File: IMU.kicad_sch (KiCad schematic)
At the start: 7 parts, among them U301 LIS3MDLTR, U302 LSM6DSOXTR

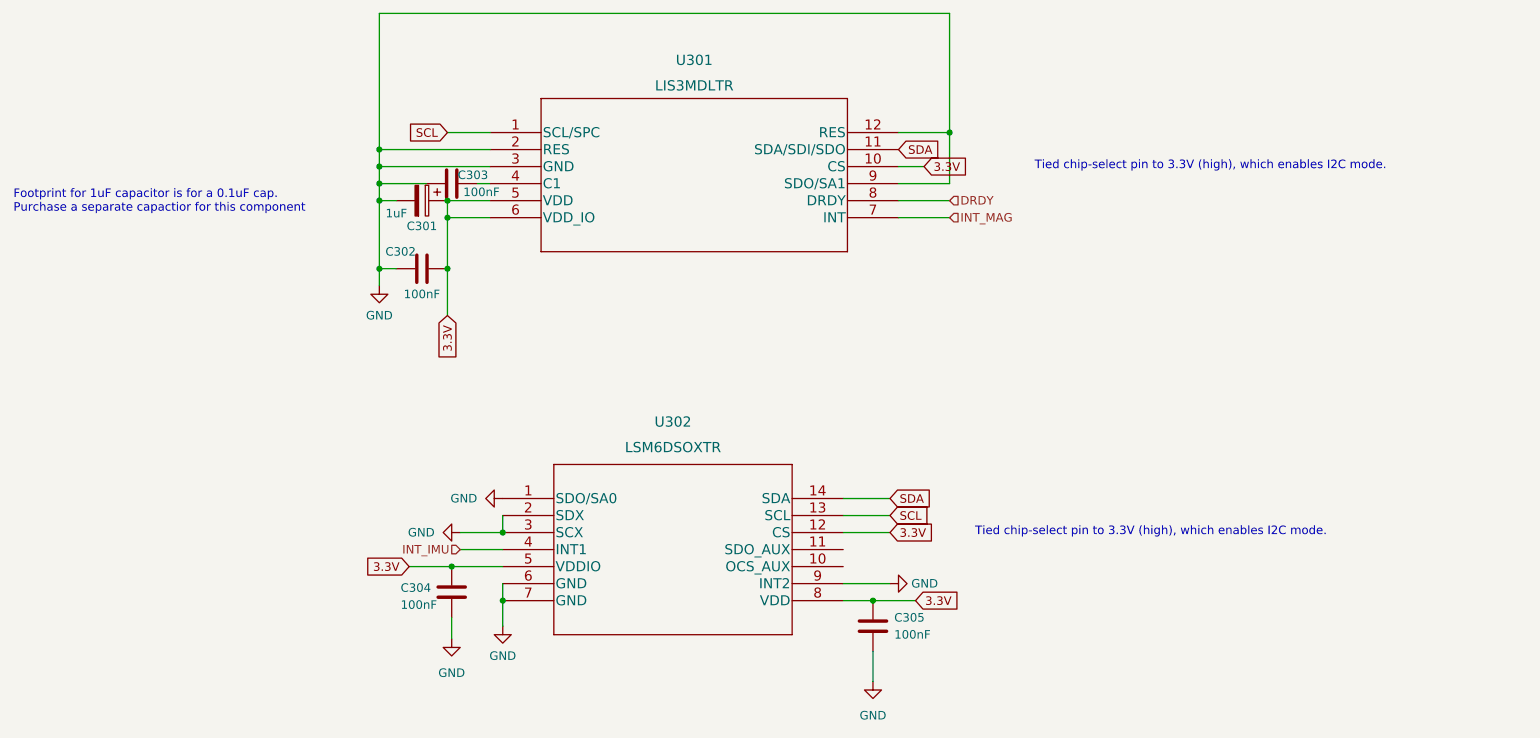
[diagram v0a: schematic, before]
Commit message: minor change to IMU schematic
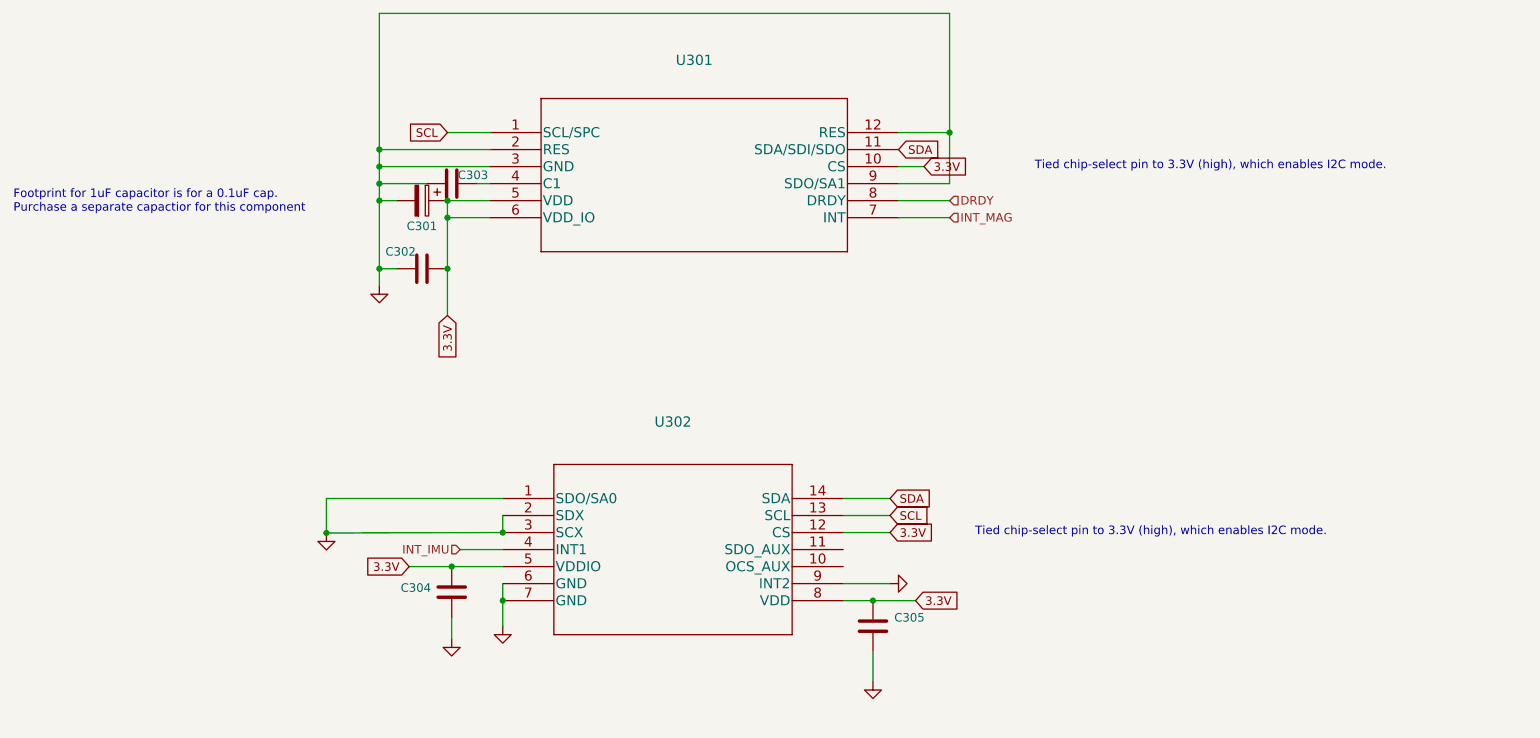
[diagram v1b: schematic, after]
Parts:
- C301: value 1uF -> (none); footprint 0.1uF P_Cap:UWP1H0R1MCL1GB -> (none)
- C302, C303, C304, C305: value 100nF -> (none); footprint Capacitor_SMD:C_0603_1608Metric_Pad1.08x0.95mm_HandSolder -> (none)
- U301: value LIS3MDLTR -> (none); footprint 3-axis magnetometer:LIS3MDLTR -> (none)
- U302: value LSM6DSOXTR -> (none); footprint 6-axis IMU:LSM6DSOXTR -> (none)
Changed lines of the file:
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@@
   (junction (at 105.41 137.795) (diameter 0) (color 0 0 0 0)
   )
+  (junction (at 79.0951 127.6916) (diameter 0) (color 0 0 0 0)
+  )
   (junction (at 105.41 127.635) (diameter 0) (color 0 0 0 0)
   )
@@
     (stroke (width 0) (type default) (color 0 0 0 0))
   )
+  (wire (pts (xy 105.41 122.555) (xy 79.0951 122.555))
+    (stroke (width 0) (type default) (color 0 0 0 0))
+  )
   (wire (pts (xy 156.21 135.255) (xy 163.195 135.255))
     (stroke (width 0) (type default) (color 0 0 0 0))
@@
     (stroke (width 0) (type default) (color 0 0 0 0))
   )
+  (wire (pts (xy 79.0951 122.555) (xy 79.0951 127.6916))
+    (stroke (width 0) (type default) (color 0 0 0 0))
+  )
   (wire (pts (xy 164.465 67.945) (xy 172.085 67.945))
     (stroke (width 0) (type default) (color 0 0 0 0))
@@
     (stroke (width 0) (type default) (color 0 0 0 0))
   )
-  (wire (pts (xy 99.06 127.635) (xy 105.41 127.635))
+  (wire (pts (xy 79.0951 127.6916) (xy 105.41 127.635))
     (stroke (width 0) (type default) (color 0 0 0 0))
   )
@@
     (in_bom yes) (on_board yes)
     (property "Reference" "C303" (id 0) (at 100.965 74.295 90))
-    (property "Value" "100nF" (id 1) (at 102.235 76.835 90))
-    (property "Footprint" "Capacitor_SMD:C_0603_1608Metric_Pad1.08x0.95mm_HandSolder" (id 2) (at 101.6 74.5998 0)
+    (property "Value" "" (id 1) (at 102.235 76.835 90))
+    (property "Footprint" "" (id 2) (at 101.6 74.5998 0)
       (effects (font (size 1.27 1.27)) hide)
     )
@@
       (effects (font (size 1.27 1.27)) (justify left))
     )
-    (property "Value" "100nF" (id 1) (at 163.83 142.8749 0)
+    (property "Value" "" (id 1) (at 163.83 142.8749 0)
       (effects (font (size 1.27 1.27)) (justify left))
     )
-    (property "Footprint" "Capacitor_SMD:C_0603_1608Metric_Pad1.08x0.95mm_HandSolder" (id 2) (at 161.6202 145.415 0)
+    (property "Footprint" "" (id 2) (at 161.6202 145.415 0)
       (effects (font (size 1.27 1.27)) hide)
     )
@@
     (pin "2")
   )
-  (symbol (lib_id "power:GND") (at 99.06 127.635 270) (unit 1)
-    (in_bom yes) (on_board yes) (fields_autoplaced)
-    (property "Reference" "#PWR0117" (id 0) (at 92.71 127.635 0)
-      (effects (font (size 1.27 1.27)) hide)
-    )
-    (property "Value" "GND" (id 1) (at 95.25 127.6349 90)
-      (effects (font (size 1.27 1.27)) (justify right))
-    )
-    (property "Footprint" "" (id 2) (at 99.06 127.635 0)
-      (effects (font (size 1.27 1.27)) hide)
-    )
-    (property "Datasheet" "" (id 3) (at 99.06 127.635 0)
-      (effects (font (size 1.27 1.27)) hide)
-    )
-    (pin "1")
-  )
-  (symbol (lib_id "power:GND") (at 105.41 122.555 270) (unit 1)
-    (in_bom yes) (on_board yes) (fields_autoplaced)
-    (property "Reference" "#PWR0122" (id 0) (at 99.06 122.555 0)
-      (effects (font (size 1.27 1.27)) hide)
-    )
-    (property "Value" "GND" (id 1) (at 101.6 122.5549 90)
-      (effects (font (size 1.27 1.27)) (justify right))
-    )
-    (property "Footprint" "" (id 2) (at 105.41 122.555 0)
-      (effects (font (size 1.27 1.27)) hide)
-    )
-    (property "Datasheet" "" (id 3) (at 105.41 122.555 0)
+  (symbol (lib_id "power:GND") (at 79.0951 127.6916 0) (unit 1)
+    (in_bom yes) (on_board yes) (fields_autoplaced)
+    (property "Reference" "#PWR0117" (id 0) (at 79.0951 134.0416 0)
+      (effects (font (size 1.27 1.27)) hide)
+    )
+    (property "Value" "" (id 1) (at 79.0951 132.2169 0))
+    (property "Footprint" "" (id 2) (at 79.0951 127.6916 0)
+      (effects (font (size 1.27 1.27)) hide)
+    )
+    (property "Datasheet" "" (id 3) (at 79.0951 127.6916 0)
       (effects (font (size 1.27 1.27)) hide)
     )
@@
       (effects (font (size 1.27 1.27)) hide)
     )
-    (property "Value" "GND" (id 1) (at 97.79 148.59 0))
+    (property "Value" "" (id 1) (at 97.79 148.59 0))
     (property "Footprint" "" (id 2) (at 97.79 143.51 0)
       (effects (font (size 1.27 1.27)) hide)
@@
       (effects (font (size 1.27 1.27)) (justify left))
     )
-    (property "Value" "100nF" (id 1) (at 90.17 138.43 0)
+    (property "Value" "" (id 1) (at 90.17 138.43 0)
       (effects (font (size 1.27 1.27)) (justify left))
     )
-    (property "Footprint" "Capacitor_SMD:C_0603_1608Metric_Pad1.08x0.95mm_HandSolder" (id 2) (at 98.7552 140.335 0)
+    (property "Footprint" "" (id 2) (at 98.7552 140.335 0)
       (effects (font (size 1.27 1.27)) hide)
     )
@@
       (effects (font (size 1.524 1.524)))
     )
-    (property "Value" "LIS3MDLTR" (id 1) (at 133.985 60.96 0)
-      (effects (font (size 1.524 1.524)))
-    )
-    (property "Footprint" "3-axis magnetometer:LIS3MDLTR" (id 2) (at 133.985 61.849 0)
+    (property "Value" "" (id 1) (at 133.985 60.96 0)
+      (effects (font (size 1.524 1.524)))
+    )
+    (property "Footprint" "" (id 2) (at 133.985 61.849 0)
       (effects (font (size 1.524 1.524)) hide)
     )
@@
       (effects (font (size 1.524 1.524)))
     )
-    (property "Value" "LSM6DSOXTR" (id 1) (at 130.81 114.935 0)
-      (effects (font (size 1.524 1.524)))
-    )
-    (property "Footprint" "6-axis IMU:LSM6DSOXTR" (id 2) (at 130.81 116.459 0)
+    (property "Value" "" (id 1) (at 130.81 114.935 0)
+      (effects (font (size 1.524 1.524)))
+    )
+    (property "Footprint" "" (id 2) (at 130.81 116.459 0)
       (effects (font (size 1.524 1.524)) hide)
     )
@@
     (in_bom yes) (on_board yes)
     (property "Reference" "C301" (id 0) (at 93.345 81.915 90))
-    (property "Value" "1uF" (id 1) (at 89.535 80.01 90))
-    (property "Footprint" "0.1uF P_Cap:UWP1H0R1MCL1GB" (id 2) (at 89.535 79.0702 0)
+    (property "Value" "" (id 1) (at 89.535 80.01 90))
+    (property "Footprint" "" (id 2) (at 89.535 79.0702 0)
       (effects (font (size 1.27 1.27)) hide)
     )
@@
       (effects (font (size 1.27 1.27)) hide)
     )
-    (property "Value" "GND" (id 1) (at 166.37 135.2549 90)
+    (property "Value" "" (id 1) (at 166.37 135.2549 90)
       (effects (font (size 1.27 1.27)) (justify right))
     )
@@
       (effects (font (size 1.27 1.27)) hide)
     )
-    (property "Value" "GND" (id 1) (at 105.41 146.05 0))
+    (property "Value" "" (id 1) (at 105.41 146.05 0))
     (property "Footprint" "" (id 2) (at 105.41 141.605 0)
       (effects (font (size 1.27 1.27)) hide)
@@
       (effects (font (size 1.27 1.27)) hide)
     )
-    (property "Value" "GND" (id 1) (at 160.655 154.94 0))
+    (property "Value" "" (id 1) (at 160.655 154.94 0))
     (property "Footprint" "" (id 2) (at 160.655 149.86 0)
       (effects (font (size 1.27 1.27)) hide)
@@
       (effects (font (size 1.27 1.27)) hide)
     )
-    (property "Value" "GND" (id 1) (at 86.995 95.25 0))
+    (property "Value" "" (id 1) (at 86.995 95.25 0))
     (property "Footprint" "" (id 2) (at 86.995 90.805 0)
       (effects (font (size 1.27 1.27)) hide)
@@
     (in_bom yes) (on_board yes)
     (property "Reference" "C302" (id 0) (at 90.17 85.725 90))
-    (property "Value" "100nF" (id 1) (at 93.345 92.075 90))
-    (property "Footprint" "Capacitor_SMD:C_0603_1608Metric_Pad1.08x0.95mm_HandSolder" (id 2) (at 89.535 89.2302 0)
+    (property "Value" "" (id 1) (at 93.345 92.075 90))
+    (property "Footprint" "" (id 2) (at 89.535 89.2302 0)
       (effects (font (size 1.27 1.27)) hide)
     )
@@
     (pin "2")
   )
+  (sheet_instances
+    (path "/" (page "1"))
+  )
+  (symbol_instances
+    (path "/56cd55ba-ffbd-4482-9959-8e6270f31458"
+      (reference "#PWR0115") (unit 1) (value "GND") (footprint "")
+    )
+    (path "/ba34d09b-b382-4b6b-9cec-0f460bf8d63b"
+      (reference "#PWR0116") (unit 1) (value "GND") (footprint "")
+    )
+    (path "/47196425-a927-4436-9557-3ad5cb9685e0"
+      (reference "#PWR0117") (unit 1) (value "GND") (footprint "")
+    )
+    (path "/bff95e99-a0c9-4fee-8607-066975a5ac9d"
+      (reference "#PWR0118") (unit 1) (value "GND") (footprint "")
+    )
+    (path "/bdf6cdd0-a083-42ed-b388-3f6b00d753ec"
+      (reference "#PWR0119") (unit 1) (value "GND") (footprint "")
+    )
+    (path "/b83d40be-f6a9-41a0-b4b1-8341ddbca8b8"
+      (reference "#PWR0123") (unit 1) (value "GND") (footprint "")
+    )
+    (path "/b1896925-e4f0-4609-9a93-4d292ecf123c"
+      (reference "C301") (unit 1) (value "1uF") (footprint "0.1uF P_Cap:UWP1H0R1MCL1GB")
+    )
+    (path "/d3966c21-8628-453d-804f-17dde56b7fa2"
+      (reference "C302") (unit 1) (value "100nF") (footprint "Capacitor_SMD:C_0603_1608Metric_Pad1.08x0.95mm_HandSolder")
+    )
+    (path "/1f9e2be9-b347-4b82-b043-52f78e1a1cc6"
+      (reference "C303") (unit 1) (value "100nF") (footprint "Capacitor_SMD:C_0603_1608Metric_Pad1.08x0.95mm_HandSolder")
+    )
+    (path "/8dca2e70-08c3-4335-9cca-0b4466330318"
+      (reference "C304") (unit 1) (value "100nF") (footprint "Capacitor_SMD:C_0603_1608Metric_Pad1.08x0.95mm_HandSolder")
+    )
+    (path "/2ce63c4c-d569-4d5d-8aee-02280476b0a8"
+      (reference "C305") (unit 1) (value "100nF") (footprint "Capacitor_SMD:C_0603_1608Metric_Pad1.08x0.95mm_HandSolder")
+    )
+    (path "/9bbeb2de-faa3-4549-a1a8-fb9d6d9975aa"
+      (reference "U301") (unit 1) (value "LIS3MDLTR") (footprint "3-axis magnetometer:LIS3MDLTR")
+    )
+    (path "/a2cd666a-262d-47f5-aa00-a6c5d5b15194"
+      (reference "U302") (unit 1) (value "LSM6DSOXTR") (footprint "6-axis IMU:LSM6DSOXTR")
+    )
+  )
 )
